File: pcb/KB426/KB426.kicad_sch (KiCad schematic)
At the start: 129 parts, among them SW1 SW_Push_45deg, SW10 SW_Push_45deg, SW11 SW_Push_45deg, SW12 SW_Push_45deg, SW13 SW_Push_45deg, SW14 SW_Push_45deg, SW15 SW_Push_45deg, SW16 SW_Push_45deg, SW17 SW_Push_45deg, SW18 SW_Push_45deg, SW19 SW_Push_45deg, SW2 SW_Push_45deg, SW20 SW_Push_45deg, SW21 SW_Push_45deg, SW22 SW_Push_45deg, SW23 SW_Push_45deg, SW24 SW_Push_45deg, SW25 SW_Push_45deg, SW26 SW_Push_45deg, SW27 SW_Push_45deg, SW28 SW_Push_45deg, SW29 SW_Push_45deg, SW3 SW_Push_45deg, SW30 SW_Push_45deg, SW31 SW_Push_45deg, SW32 SW_Push_45deg, SW33 SW_Push_45deg, SW34 SW_Push_45deg, SW35 SW_Push_45deg, SW36 SW_Push_45deg, SW37 SW_Push_45deg, SW38 SW_Push_45deg, SW39 SW_Push_45deg, SW4 SW_Push_45deg, SW40 SW_Push_45deg, SW41 SW_Push_45deg, SW42 SW_Push_45deg, SW43 SW_Push_45deg, SW44 SW_Push_45deg, SW45 SW_Push_45deg, SW46 SW_Push_45deg, SW47 SW_Push_45deg, SW48 SW_Push_45deg, SW49 SW_Push_45deg, SW5 SW_Push_45deg, SW50 SW_Push_45deg, SW51 SW_Push_45deg, SW52 SW_Push_45deg, SW53 SW_Push_45deg, SW54 SW_Push_45deg, SW55 SW_Push_45deg, SW56 SW_Push_45deg, SW57 SW_Push_45deg, SW58 SW_Push_45deg, SW59 SW_Push_45deg, SW6 SW_Push_45deg, SW60 SW_Push_45deg, SW61 SW_Push_45deg, SW62 SW_Push_45deg, SW63 SW_Push_45deg, SW64 SW_Push_45deg, SW7 SW_Push_45deg, SW8 SW_Push_45deg, SW9 SW_Push_45deg, U1 Pico

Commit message: + update sch and pcb
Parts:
- SW47: footprint PCM_Switch_Keyboard_Cherry_MX:SW_Cherry_MX_PCB_2.00u -> PCM_Switch_Keyboard_Cherry_MX:SW_Cherry_MX_PCB_1.00u
- SW56: footprint PCM_Switch_Keyboard_Cherry_MX:SW_Cherry_MX_PCB_1.00u -> PCM_Switch_Keyboard_Cherry_MX:SW_Cherry_MX_PCB_2.00u
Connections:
- net Column 0: no longer names the net of SW1.2, SW17.2, SW25.2, SW33.2, SW41.2, SW49.2, SW57.2, SW9.2, U1.11 (GPIO8)
- net Column 1: no longer names the net of SW10.2, SW18.2, SW2.2, SW26.2, SW34.2, SW42.2, SW50.2, SW58.2, U1.12 (GPIO9)
- net Column 2: no longer names the net of SW11.2, SW19.2, SW27.2, SW3.2, SW35.2, SW43.2, SW51.2, SW59.2, U1.14 (GPIO10)
- net Column 3: no longer names the net of SW12.2, SW20.2, SW28.2, SW36.2, SW4.2, SW44.2, SW52.2, SW60.2, U1.15 (GPIO11)
- net Column 4: no longer names the net of SW13.2, SW21.2, SW29.2, SW37.2, SW45.2, SW5.2, SW53.2, SW61.2, U1.16 (GPIO12)
- net Column 5: no longer names the net of SW14.2, SW22.2, SW30.2, SW38.2, SW46.2, SW54.2, SW6.2, SW62.2, U1.17 (GPIO13)
- net Column 6: no longer names the net of SW15.2, SW23.2, SW31.2, SW39.2, SW7.2, U1.19 (GPIO14)
- net Column 6: now also SW47.2, SW55.2, SW63.2; no longer SW48.2, SW56.2, SW64.2
- net Column 7: no longer names the net of SW16.2, SW24.2, SW32.2, SW40.2, SW8.2, U1.20 (GPIO15)
- net Column 7: now also SW48.2, SW56.2, SW64.2; no longer SW47.2, SW55.2, SW63.2
- net Row 0: no longer names the net of D1.1 (K), D2.1 (K), D3.1 (K), D4.1 (K), D5.1 (K), D6.1 (K), D7.1 (K), D8.1 (K)
- net Row 0: now also U1.6 (GPIO4); no longer U1.1 (GPIO0)
- net Row 1: no longer names the net of D10.1 (K), D11.1 (K), D12.1 (K), D13.1 (K), D14.1 (K), D15.1 (K), D16.1 (K), D9.1 (K)
- net Row 1: now also U1.5 (GPIO3); no longer U1.2 (GPIO1)
- net Row 2: no longer names the net of D17.1 (K), D18.1 (K), D19.1 (K), D20.1 (K), D21.1 (K), D22.1 (K), D23.1 (K), D24.1 (K), U1.4 (GPIO2)
- net Row 3: no longer names the net of D25.1 (K), D26.1 (K), D27.1 (K), D28.1 (K), D29.1 (K), D30.1 (K), D31.1 (K), D32.1 (K)
- net Row 3: now also U1.2 (GPIO1); no longer U1.5 (GPIO3)
- net Row 4: no longer names the net of D33.1 (K), D34.1 (K), D35.1 (K), D36.1 (K), D37.1 (K), D38.1 (K), D39.1 (K), D40.1 (K)
- net Row 4: now also U1.1 (GPIO0); no longer U1.6 (GPIO4)
- net Row 5: no longer names the net of D41.1 (K), D42.1 (K), D43.1 (K), D44.1 (K), D45.1 (K), D46.1 (K), D47.1 (K), D48.1 (K)
- net Row 5: now also U1.10 (GPIO7); no longer U1.7 (GPIO5)
- net Row 6: no longer names the net of D49.1 (K), D50.1 (K), D51.1 (K), D52.1 (K), D53.1 (K), D54.1 (K), D55.1 (K), D56.1 (K), U1.9 (GPIO6)
- net Row 7: no longer names the net of D57.1 (K), D58.1 (K), D59.1 (K), D60.1 (K), D61.1 (K), D62.1 (K), D63.1 (K), D64.1 (K)
- net Row 7: now also U1.7 (GPIO5); no longer U1.10 (GPIO7)
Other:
- moved on the sheet: D33, D34, D35, D36, D37, D38, D39, D40, D47, D48, D55, D56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

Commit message: + update pcb
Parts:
- added SSD1331_SPI1: ~, OLED_Display_SSD1331_SPI:OLED_Display_SSD1331_SPI, symbol OLED_Display_SSD1331_SPI:OLED_Display_SSD1331_SPI
- added SW65: RotaryEncoder_Switch, Rotary_Encoder:RotaryEncoder_Alps_EC11E-Switch_Vertical_H20mm, symbol Device:RotaryEncoder_Switch
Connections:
- net Row 8: now reaches D57.1 (K), D58.1 (K), D59.1 (K), D60.1 (K), D61.1 (K), D62.1 (K), D63.1 (K), D64.1 (K)
- net Row 8: now also U1.20 (GPIO15); no longer U1.7 (GPIO5)
- net Col 4: now reaches SW12.2, SW20.2, SW28.2, SW36.2, SW4.2, SW44.2, SW52.2, SW60.2
- net Col 4: now also U1.5 (GPIO3); no longer U1.15 (GPIO11)
- net Row 7: now reaches D49.1 (K), D50.1 (K), D51.1 (K), D52.1 (K), D53.1 (K), D54.1 (K), D55.1 (K), D56.1 (K)
- net Row 7: now also U1.19 (GPIO14); no longer U1.9 (GPIO6)
- net Row 3: now reaches D17.1 (K), D18.1 (K), D19.1 (K), D20.1 (K), D21.1 (K), D22.1 (K), D23.1 (K), D24.1 (K)
- net Row 3: now also U1.14 (GPIO10); no longer U1.4 (GPIO2)
- net Col 3: now reaches SW11.2, SW19.2, SW27.2, SW3.2, SW35.2, SW43.2, SW51.2, SW59.2
- net Col 3: now also U1.4 (GPIO2); no longer U1.14 (GPIO10)
- net Col 2: now reaches SW10.2, SW18.2, SW2.2, SW26.2, SW34.2, SW42.2, SW50.2, SW58.2
- net Col 2: now also U1.2 (GPIO1); no longer U1.12 (GPIO9)
- net Row 2: now reaches D10.1 (K), D11.1 (K), D12.1 (K), D13.1 (K), D14.1 (K), D15.1 (K), D16.1 (K), D9.1 (K)
- net Row 2: now also U1.12 (GPIO9); no longer U1.5 (GPIO3)
- net Col 5: now reaches SW13.2, SW21.2, SW29.2, SW37.2, SW45.2, SW5.2, SW53.2, SW61.2
- net Col 5: now also U1.6 (GPIO4); no longer U1.16 (GPIO12)
- net Col 8: now reaches SW16.2, SW24.2, SW32.2, SW40.2, SW48.2, SW56.2, SW64.2, SW8.2
- net Col 8: now also U1.10 (GPIO7); no longer U1.20 (GPIO15)
- net Row 5: now reaches D33.1 (K), D34.1 (K), D35.1 (K), D36.1 (K), D37.1 (K), D38.1 (K), D39.1 (K), D40.1 (K)
- net Row 5: now also U1.16 (GPIO12); no longer U1.1 (GPIO0)
- net Row 6: now reaches D41.1 (K), D42.1 (K), D43.1 (K), D44.1 (K), D45.1 (K), D46.1 (K), D47.1 (K), D48.1 (K)
- net Row 6: now also U1.17 (GPIO13); no longer U1.10 (GPIO7)
- net Col 1: now reaches SW1.2, SW17.2, SW25.2, SW33.2, SW41.2, SW49.2, SW57.2, SW9.2
- net Col 1: now also U1.1 (GPIO0); no longer U1.11 (GPIO8)
- net Col 6: now reaches SW14.2, SW22.2, SW30.2, SW38.2, SW46.2, SW54.2, SW6.2, SW62.2
- net Col 6: now also U1.7 (GPIO5); no longer U1.17 (GPIO13)
- net Col 7: now reaches SW15.2, SW23.2, SW31.2, SW39.2, SW47.2, SW55.2, SW63.2, SW7.2
- net Col 7: now also U1.9 (GPIO6); no longer U1.19 (GPIO14)
- net Row 4: now reaches D25.1 (K), D26.1 (K), D27.1 (K), D28.1 (K), D29.1 (K), D30.1 (K), D31.1 (K), D32.1 (K)
- net Row 4: now also U1.15 (GPIO11); no longer U1.2 (GPIO1)
- net at U1.21 (GPIO16): now also SSD1331_SPI1. (VCC)
- net at U1.22 (GPIO17): now also SSD1331_SPI1. (VCC)
- net at U1.24 (GPIO18): now also SSD1331_SPI1. (VCC)
- net at U1.25 (GPIO19): now also SSD1331_SPI1. (VCC)
- net at U1.26 (GPIO20): now also SSD1331_SPI1. (VCC)
- net at U1.31 (GPIO26_ADC0): now also SW65.S2
- net at U1.32 (GPIO27_ADC1): now also SW65.B
- net at U1.34 (GPIO28_ADC2): now also SW65.A
- net GND: now reaches U1.38 (GND)
- net GND: now also SSD1331_SPI1. (VCC), SW65.C, SW65.S1
- net VBUS: now reaches U1.40 (VBUS)
- net VBUS: now also SSD1331_SPI1. (VCC)
- net Row 1: now reaches D1.1 (K), D2.1 (K), D3.1 (K), D4.1 (K), D5.1 (K), D6.1 (K), D7.1 (K), D8.1 (K)
- net Row 1: now also U1.11 (GPIO8); no longer U1.6 (GPIO4)
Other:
- note added: "CLK"
- note added: "DT"
- moved on the sheet: D33, D34, D35, D37, SW33, SW34, SW35, U1

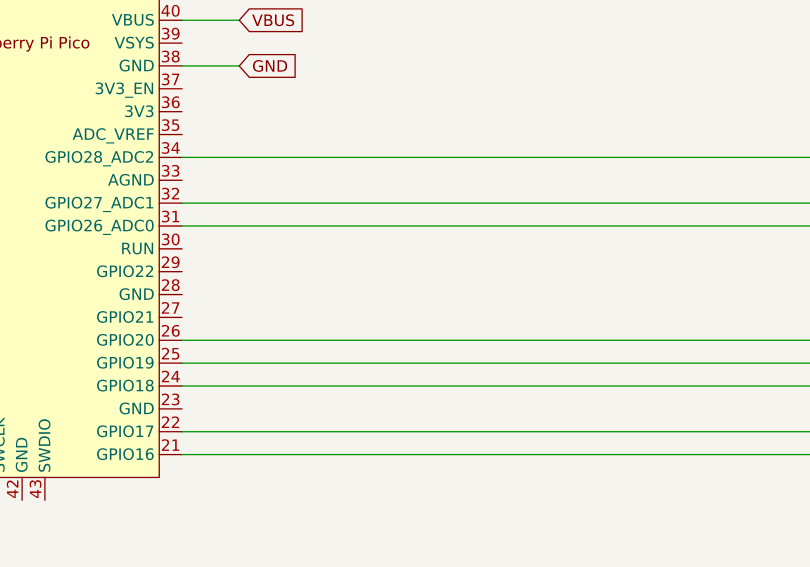
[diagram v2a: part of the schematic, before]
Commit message: + update pcb and schematic (add led)
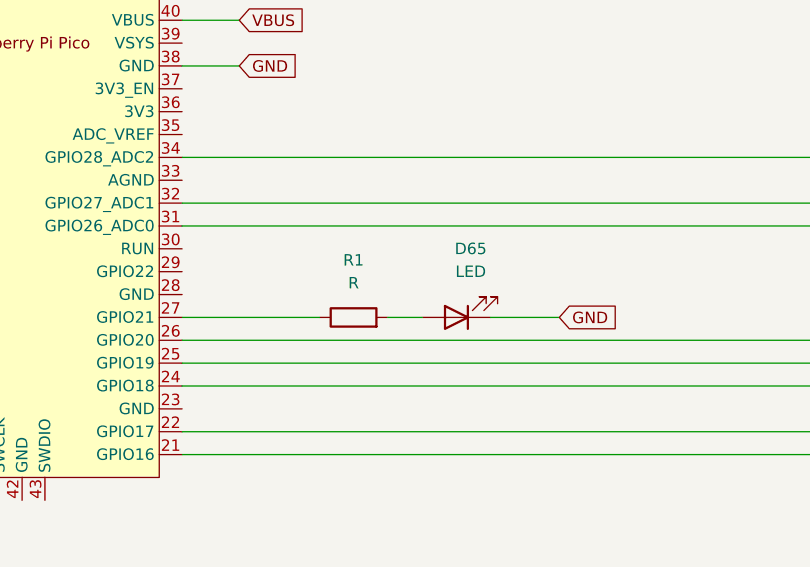
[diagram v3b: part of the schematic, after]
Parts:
- added D65: LED, LED_THT:LED_D5.0mm, symbol Device:LED
- added R1: R, Resistor_THT:R_Axial_DIN0207_L6.3mm_D2.5mm_P10.16mm_Horizontal, symbol Device:R
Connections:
- net GND: now also D65.1 (K)
- net at U1.27 (GPIO21): now also R1.1
- new net: D65.2 (A), R1.2
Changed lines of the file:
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@@
 	(wire
 		(pts
+			(xy 201.93 81.28) (xy 205.74 81.28)
+		)
+		(stroke
+			(width 0)
+			(type default)
+		)
+	)
+	(wire
+		(pts
 			(xy 93.98 144.78) (xy 119.38 144.78)
 		)
@@
 	(wire
 		(pts
+			(xy 179.07 81.28) (xy 194.31 81.28)
+		)
+		(stroke
+			(width 0)
+			(type default)
+		)
+	)
+	(wire
+		(pts
 			(xy 254 167.64) (xy 254 149.86)
 		)
@@
 	(wire
 		(pts
+			(xy 213.36 81.28) (xy 220.98 81.28)
+		)
+		(stroke
+			(width 0)
+			(type default)
+		)
+	)
+	(wire
+		(pts
 			(xy 138.43 73.66) (xy 143.51 73.66)
 		)
@@
 		)
 	)
+	(global_label "GND"
+		(shape input)
+		(at 220.98 81.28 0)
+		(fields_autoplaced yes)
+		(effects
+			(font
+				(size 1.27 1.27)
+			)
+			(justify left)
+		)
+		(property "Intersheetrefs" "${INTERSHEET_REFS}"
+			(at 227.8357 81.28 0)
+			(effects
+				(font
+					(size 1.27 1.27)
+				)
+				(justify left)
+				(hide yes)
+			)
+		)
+	)
 	(global_label "Row 7"
 		(shape input)
@@
 	)
 	(symbol
+		(lib_id "Device:LED")
+		(at 209.55 81.28 180)
+		(unit 1)
+		(exclude_from_sim no)
+		(in_bom yes)
+		(on_board yes)
+		(dnp no)
+		(fields_autoplaced yes)
+		(property "Reference" "D65"
+			(at 211.1375 73.66 0)
+			(effects
+				(font
+					(size 1.27 1.27)
+				)
+			)
+		)
+		(property "Value" "LED"
+			(at 211.1375 76.2 0)
+			(effects
+				(font
+					(size 1.27 1.27)
+				)
+			)
+		)
+		(property "Footprint" "LED_THT:LED_D5.0mm"
+			(at 209.55 81.28 0)
+			(effects
+				(font
+					(size 1.27 1.27)
+				)
+				(hide yes)
+			)
+		)
+		(property "Datasheet" "~"
+			(at 209.55 81.28 0)
+			(effects
+				(font
+					(size 1.27 1.27)
+				)
+				(hide yes)
+			)
+		)
+		(property "Description" "Light emitting diode"
+			(at 209.55 81.28 0)
+			(effects
+				(font
+					(size 1.27 1.27)
+				)
+				(hide yes)
+			)
+		)
+		(pin "1"
+		)
+		(pin "2"
+		)
+		(instances
+			(project "KB426"
+				(path "/9a9ef932-5886-4734-ab54-818112b62564"
+					(reference "D65")
+					(unit 1)
+				)
+			)
+		)
+	)
+	(symbol
 		(lib_id "Switch:SW_Push_45deg")
 		(at 274.32 134.62 90)
@@
 					(unit 1)
 				)
+			)
+		)
+	)
+	(symbol
+		(lib_id "Device:R")
+		(at 198.12 81.28 90)
+		(unit 1)
+		(exclude_from_sim no)
+		(in_bom yes)
+		(on_board yes)
+		(dnp no)
+		(fields_autoplaced yes)
+		(property "Reference" "R1"
+			(at 198.12 74.93 90)
+			(effects
+				(font
+					(size 1.27 1.27)
+				)
+			)
+		)
+		(property "Value" "R"
+			(at 198.12 77.47 90)
+			(effects
+				(font
+					(size 1.27 1.27)
+				)
+			)
+		)
+		(property "Footprint" "Resistor_THT:R_Axial_DIN0207_L6.3mm_D2.5mm_P10.16mm_Horizontal"
+			(at 198.12 83.058 90)
+			(effects
+				(font
+					(size 1.27 1.27)
+				)
+				(hide yes)
+			)
+		)
+		(property "Datasheet" "~"
+			(at 198.12 81.28 0)
+			(effects
+				(font
+					(size 1.27 1.27)
+				)
+				(hide yes)
+			)
+		)
+		(property "Description" "Resistor"
+			(at 198.12 81.28 0)
+			(effects
+				(font
+					(size 1.27 1.27)
+				)
+				(hide yes)
+			)
+		)
+		(pin "1"
+		)
+		(pin "2"
+		)
+		(instances
+			(project "KB426"
+				(path "/9a9ef932-5886-4734-ab54-818112b62564"
+					(reference "R1")
+					(unit 1)
+				)

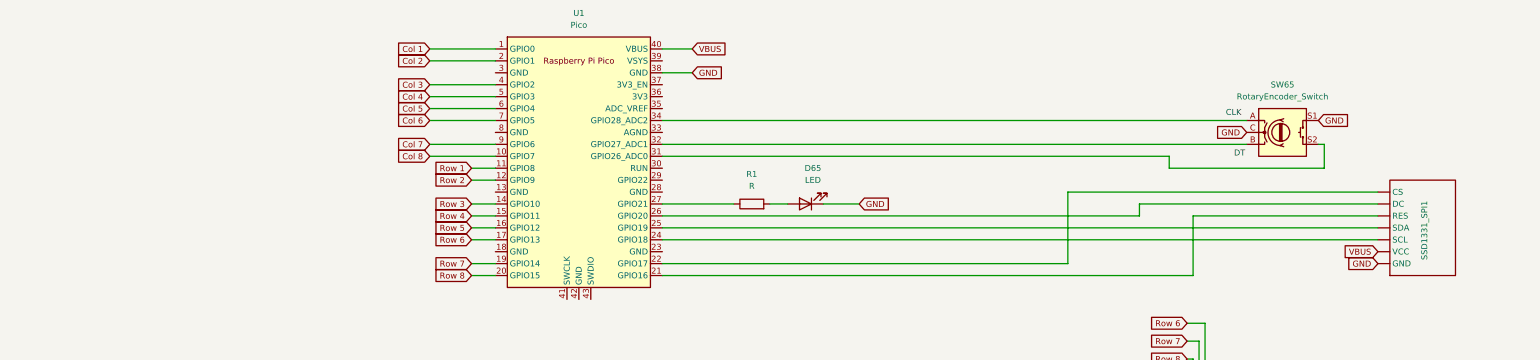
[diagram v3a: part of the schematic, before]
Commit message: update pcb (remove one led and ssd1331 spi)
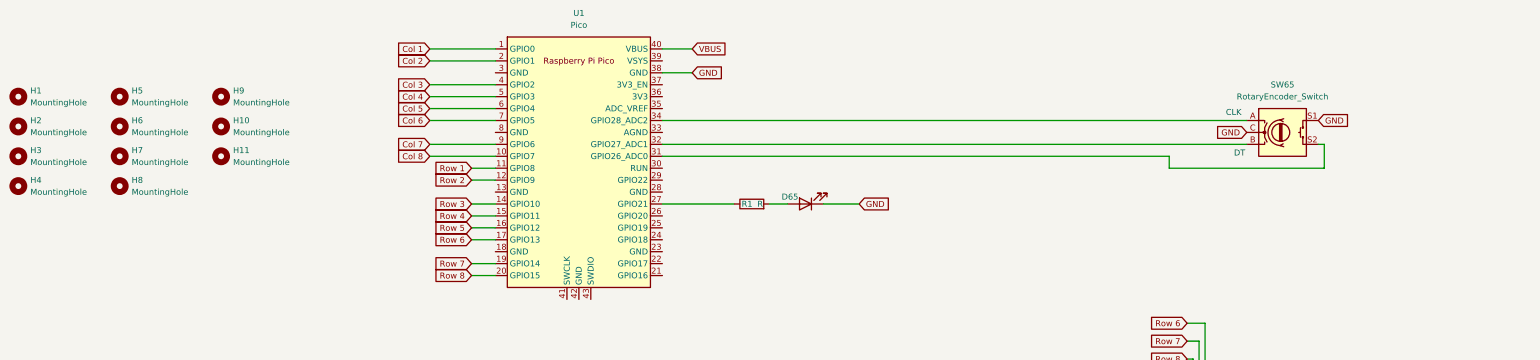
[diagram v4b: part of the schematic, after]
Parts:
- removed SSD1331_SPI1: ~, OLED_Display_SSD1331_SPI:OLED_Display_SSD1331_SPI, symbol OLED_Display_SSD1331_SPI:OLED_Display_SSD1331_SPI
- added H1, H10, H11, H2, H3, H4, H5, H6, H7, H8, H9: MountingHole, MountingHole:MountingHole_2.2mm_M2_Pad, symbol Mechanical:MountingHole
- SW55: footprint PCM_Switch_Keyboard_Cherry_MX:SW_Cherry_MX_PCB_1.00u -> PCM_Switch_Keyboard_Cherry_MX:SW_Cherry_MX_PCB_2.00u
- SW56: footprint PCM_Switch_Keyboard_Cherry_MX:SW_Cherry_MX_PCB_2.00u -> PCM_Switch_Keyboard_Cherry_MX:SW_Cherry_MX_PCB_1.00u

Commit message: + update pcb (redo all the layout)
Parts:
- removed SW47: SW_Push_45deg, PCM_Switch_Keyboard_Cherry_MX:SW_Cherry_MX_PCB_1.00u, symbol Switch:SW_Push_45deg
- added D65, D66, D67, D68, D69, D70, D71, D72: 1N4148, Diode_THT:D_DO-35_SOD27_P7.62mm_Horizontal, symbol Diode:1N4148
- added ST7735S_80x160_SPI1: ~, SPI_Displays:ST7735S_80x160_SPI, symbol SPI_Displays:ST7735S_80x160_SPI
- added SW65, SW66, SW67, SW68, SW70, SW71, SW72: SW_Push_45deg, PCM_Switch_Keyboard_Cherry_MX:SW_Cherry_MX_PCB_1.00u, symbol Switch:SW_Push_45deg
- added SW69: SW_Push_45deg, PCM_Switch_Keyboard_Cherry_MX:SW_Cherry_MX_PCB_2.00u, symbol Switch:SW_Push_45deg
- added SW_RESET1: SW_Push, Button_Switch_THT:SW_PUSH_6mm, symbol Switch:SW_Push
- SW46, SW62: footprint PCM_Switch_Keyboard_Cherry_MX:SW_Cherry_MX_PCB_1.00u -> PCM_Switch_Keyboard_Cherry_MX:SW_Cherry_MX_PCB_2.00u
- SW55: footprint PCM_Switch_Keyboard_Cherry_MX:SW_Cherry_MX_PCB_2.00u -> PCM_Switch_Keyboard_Cherry_MX:SW_Cherry_MX_PCB_1.00u
- renumbered D65 to D100, SW65 to SW47
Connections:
- net Col 1: now also SW65.2
- net Col 2: now also SW66.2
- net Col 3: now also SW67.2
- net Col 4: now also SW68.2
- net Col 5: now also SW69.2
- net Col 6: now also SW70.2
- net Col 7: now also SW47.S1, SW71.2
- net Col 8: now also SW72.2
- net GND: now also U1.13 (GND), U1.18 (GND), U1.23 (GND), U1.28 (GND), U1.3 (GND), U1.8 (GND), ST7735S_80x160_SPI1.1 (GND), SW_RESET1.2; no longer SW47.S1
- net at U1.22 (GPIO17): now also ST7735S_80x160_SPI1.7 (CS)
- net at U1.24 (GPIO18): now also ST7735S_80x160_SPI1.3 (SCL)
- net at U1.25 (GPIO19): now also ST7735S_80x160_SPI1.4 (SDA)
- net at U1.26 (GPIO20): now also ST7735S_80x160_SPI1.5 (RES)
- net at U1.27 (GPIO21): now also ST7735S_80x160_SPI1.6 (DC); no longer R1.1
- net at U1.29 (GPIO22): now also R1.1
- net at U1.30 (RUN): now also SW_RESET1.1
- net at U1.31 (GPIO26_ADC0): no longer SW47.S2
- net Rot CLK: now reaches U1.32 (GPIO27_ADC1)
- net Rot CLK: now also SW47.A; no longer SW47.B
- net Rot DT: now reaches U1.34 (GPIO28_ADC2)
- net Rot DT: now also SW47.B; no longer SW47.A
- net 3V3: now reaches U1.36 (3V3)
- net 3V3: now also ST7735S_80x160_SPI1.2 (VCC)
- net at D47.2 (A): now also SW47.S2
- new net: D67.2 (A), SW67.1
- new net: D71.2 (A), SW71.1
- new net: D69.2 (A), SW69.1
- new net: D70.2 (A), SW70.1
- new net: D72.2 (A), SW72.1
- new net: D68.2 (A), SW68.1
- new net: D66.2 (A), SW66.1
- new net: D65.2 (A), SW65.1
- new net Row 9: D65.1 (K), D66.1 (K), D67.1 (K), D68.1 (K), D69.1 (K), D70.1 (K), D71.1 (K), D72.1 (K)
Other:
- moved on the sheet: D1, D10, D100, D11, D12, D13, D14, D15, D16, D17, D18, D19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

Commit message: + update pcb
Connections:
- net Col 7: now also SW47.S2; no longer SW47.S1
- net at D47.2 (A): now also SW47.S1; no longer SW47.S2
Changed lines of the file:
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@@
-	(wire
-		(pts
-			(xy 477.52 149.86) (xy 473.71 149.86)
-		)
-		(stroke
-			(width 0)
-			(type default)
-		)
-	)
 	(wire
 		(pts
@@
 	(wire
 		(pts
+			(xy 468.63 154.94) (xy 473.71 154.94)
+		)
+		(stroke
+			(width 0)
+			(type default)
+		)
+	)
+	(wire
+		(pts
 			(xy 398.78 153.67) (xy 401.32 153.67)
 		)
@@
 	(wire
 		(pts
-			(xy 468.63 129.54) (xy 468.63 158.75)
-		)
-		(stroke
-			(width 0)
-			(type default)
-		)
-	)
-	(wire
-		(pts
 			(xy 254 189.23) (xy 254 171.45)
 		)
@@
 	(wire
 		(pts
+			(xy 473.71 154.94) (xy 473.71 129.54)
+		)
+		(stroke
+			(width 0)
+			(type default)
+		)
+	)
+	(wire
+		(pts
 			(xy 452.12 153.67) (xy 452.12 171.45)
 		)
@@
 	(wire
 		(pts
-			(xy 473.71 149.86) (xy 473.71 129.54)
-		)
-		(stroke
-			(width 0)
-			(type default)
-		)
-	)
-	(wire
-		(pts
 			(xy 219.71 88.9) (xy 179.07 88.9)
 		)
@@
 	(wire
 		(pts
+			(xy 468.63 149.86) (xy 477.52 149.86)
+		)
+		(stroke
+			(width 0)
+			(type default)
+		)
+	)
+	(wire
+		(pts
 			(xy 179.07 68.58) (xy 182.88 68.58)
 		)
@@
 	(wire
 		(pts
+			(xy 468.63 158.75) (xy 468.63 154.94)
+		)
+		(stroke
+			(width 0)
+			(type default)
+		)
+	)
+	(wire
+		(pts
 			(xy 322.58 171.45) (xy 325.12 171.45)
 		)
@@
 		)
 		(stroke
+			(width 0)
+			(type default)
+		)
+	)
+	(wire
+		(pts
+			(xy 468.63 129.54) (xy 468.63 149.86)
+		)
+		(stroke

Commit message: + update pcb, usb C hack
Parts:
- added P1: USB_C_Plug_USB2.0, symbol Connector:USB_C_Plug_USB2.0
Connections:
- net Rot CLK: now also SW47.B; no longer SW47.A
- net Rot DT: now also SW47.A; no longer SW47.B
- net Row 9: now also U1.21 (GPIO16)
- net VBUS: now also P1.A4 (VBUS), P1.A9 (VBUS), P1.B4 (VBUS), P1.B9 (VBUS)
- new net TP1: P1.A1 (GND), P1.A12 (GND), P1.B1 (GND), P1.B12 (GND), P1.S1 (SHIELD)
- new net TP2: P1.A6 (D+)
- new net TP3: P1.A7 (D-)
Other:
- moved on the sheet: D100, H1, H10, H11, H2, H3, H4, H5, H6, H7, H8, H9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

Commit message: + update pcb (qwerty layout)
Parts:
- removed D69, D70, D71, D72: 1N4148, Diode_THT:D_DO-35_SOD27_P7.62mm_Horizontal, symbol Diode:1N4148
- removed P1: USB_C_Plug_USB2.0, symbol Connector:USB_C_Plug_USB2.0
- removed SW69: SW_Push_45deg, PCM_Switch_Keyboard_Cherry_MX:SW_Cherry_MX_PCB_2.00u, symbol Switch:SW_Push_45deg
- removed SW70, SW71, SW72: SW_Push_45deg, PCM_Switch_Keyboard_Cherry_MX:SW_Cherry_MX_PCB_1.00u, symbol Switch:SW_Push_45deg
- added C1, C2: 0.01 µf, Capacitor_SMD:C_1206_3216Metric_Pad1.33x1.80mm_HandSolder, symbol Device:C
- added J1: Conn_01x03_Socket, Connector_PinHeader_2.54mm:PinHeader_1x03_P2.54mm_Vertical, symbol Connector:Conn_01x03_Socket
- added R1, R2, R3, R4: 10k, Resistor_THT:R_Axial_DIN0207_L6.3mm_D2.5mm_P10.16mm_Horizontal, symbol Device:R
- R5: renamed from R1; value R -> 390
- SW17, SW68: footprint PCM_Switch_Keyboard_Cherry_MX:SW_Cherry_MX_PCB_1.00u -> PCM_Switch_Keyboard_Cherry_MX:SW_Cherry_MX_PCB_1.75u
- SW25, SW61: footprint PCM_Switch_Keyboard_Cherry_MX:SW_Cherry_MX_PCB_1.00u -> PCM_Switch_Keyboard_Cherry_MX:SW_Cherry_MX_PCB_2.25u
- SW33, SW34, SW35: footprint PCM_Switch_Keyboard_Cherry_MX:SW_Cherry_MX_PCB_1.00u -> PCM_Switch_Keyboard_Cherry_MX:SW_Cherry_MX_PCB_1.25u
- SW36: footprint PCM_Switch_Keyboard_Cherry_MX:SW_Cherry_MX_PCB_6.00u -> PCM_Switch_Keyboard_Cherry_MX:SW_Cherry_MX_PCB_6.25u
- SW54, SW9: footprint PCM_Switch_Keyboard_Cherry_MX:SW_Cherry_MX_PCB_1.00u -> PCM_Switch_Keyboard_Cherry_MX:SW_Cherry_MX_PCB_1.50u
- SW62: footprint PCM_Switch_Keyboard_Cherry_MX:SW_Cherry_MX_PCB_2.00u -> PCM_Switch_Keyboard_Cherry_MX:SW_Cherry_MX_PCB_1.00u
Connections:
- net GND: now also U1.42 (GND), C1.2, C2.2, J1.2 (Pin_2)
- net Rot CLK: now also C1.1, R3.1; no longer SW47.B
- net Rot DT: now also C2.1, R4.1; no longer SW47.A
- net Row 6: now also D64.1 (K); no longer D48.1 (K)
- net Row 8: now also D48.1 (K); no longer D64.1 (K)
- net at U1.41 (SWCLK): now also J1.3 (Pin_3)
- net at U1.43 (SWDIO): now also J1.1 (Pin_1)
- net 3V3 renamed +3V3
- net +3V3: now also R1.1, R2.1
- net VBUS renamed +5V
- new net: R2.2, R4.2, SW47.A
- new net: R1.2, R3.2, SW47.B
- no-connect marks 0 -> 1
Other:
- moved on the sheet: D48, D64, SW48, SW64
